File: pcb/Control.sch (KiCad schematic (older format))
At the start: 13 parts, among them U1 ATMEGA328, U2 FT231X, Y1 Cristal

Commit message: carga de hojas jerarquia
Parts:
- added C11: 4,7u, symbol CP1
- added C12, C15: 100n, symbol C
- added U?: PCA9685, symbol PCA9685
- D1, D2: value LED -> Rojo; Fabricante (none) -> KINGBRIGHT ELECTRONIC; Provedor (none) -> tme; Ref (none) -> KP-2012EC; Ref_Proveedor (none) -> KP-2012EC
- R4, R5: value R -> 270; Fabricante (none) -> vishay; Provedor (none) -> tme; Ref (none) -> CRCW0805270RFKTABC; Ref_Proveedor (none) -> CRCW0805270RFKTABC
- U1: symbol ATMEGA328 -> ATMEGA328-RESCUE-ATMEGA328_Motor_Board; Fabricante (none) -> atmel; Provedor (none) -> tme; Ref (none) -> ATMEGA328P-AU; Ref_Proveedor (none) -> ATMEGA328P-AU
- U2: Fabricante (none) -> ftdi; Provedor (none) -> tme; Ref (none) -> FT231XS-R; Ref_Proveedor (none) -> FT231XS-R
- Y1: value Cristal -> 16MHz; Proveedor (none) -> tme; Ref. Proveedor (none) -> EEVFK1J471M
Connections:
- wire segments 80 -> 91
- no-connect marks 10 -> 8
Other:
- note added: "Rx"
- note added: "Tx"
- moved on the sheet: C2, C3, D1, D2, R1, R2, R3, R4, R5, U2, Y1

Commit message: finalizada realizacion de esquema
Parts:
- removed C1: CP1, symbol CP1
- removed C11: 4,7u, symbol CP1
- added C1: 4,7u, symbol CP
- added C3, C6: CP, symbol CP
- added C4: 100n, symbol C
- added R2, R3: 1K, symbol R
- added R4: 10K, symbol R
- added SW1: Pulsador_4p, symbol Pulsador_4p
- gave numbers to parts that had none: 1
- renumbered C15 to C5, C12 to C7, C3 to C8, R2 to R5, R3 to R6, R4 to R7, R5 to R8, U2 to U3
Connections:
- net labels added: ENC1_A2, ENC1_B2, ENC2_A2, ENC2_B2, MOTOR1_CURRENT, MOTOR2_CURRENT, MOTOR3_CURRENT, MOTOR4_CURRENT, PWM_OE, SCL, SDA, SERVO1, SERVO2, SERVO3, SERVO4
- net labels removed: CONSIGNA3, CONSIGNA4, DIO_1, DIO_2, DIO_3, DIO_4, DIO_5, DIO_6, DIO_7, DIO_8, MOTOR1_SENSE, MOTOR2_SENSE, MOTOR3_SENSE, MOTOR4_SENSE
- wire segments 91 -> 122
- no-connect marks 8 -> 13
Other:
- moved on the sheet: C2, R1, R5, R6, U1, U2, Y1

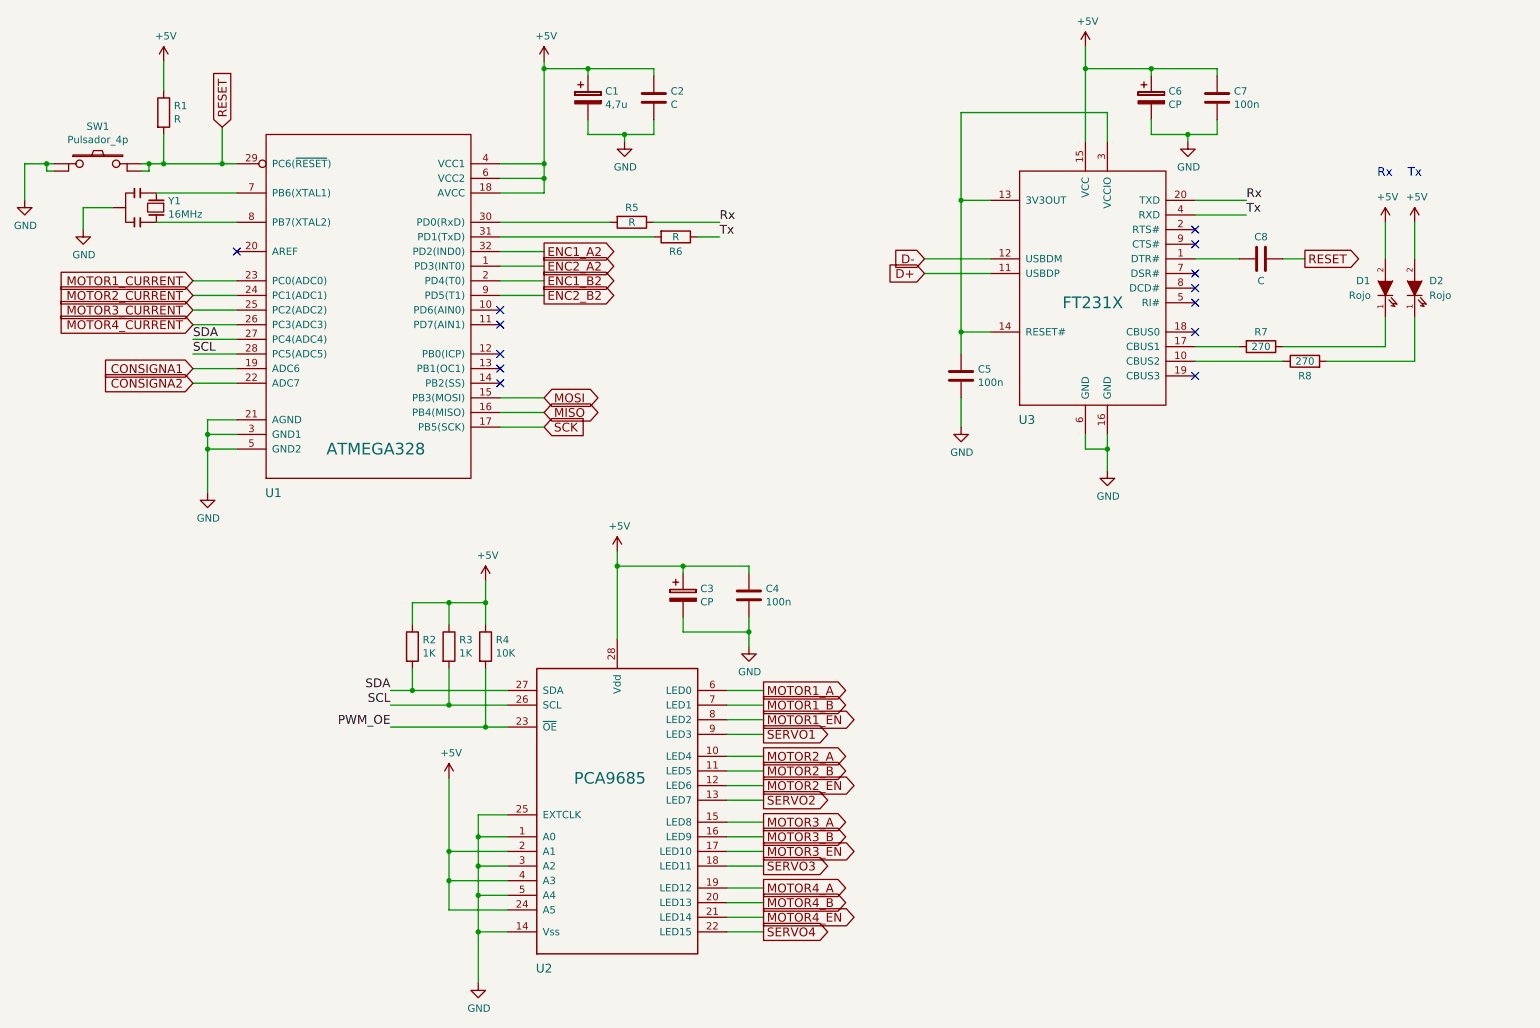
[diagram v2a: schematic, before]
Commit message: asociacion de huellas a resistencias y condensadores
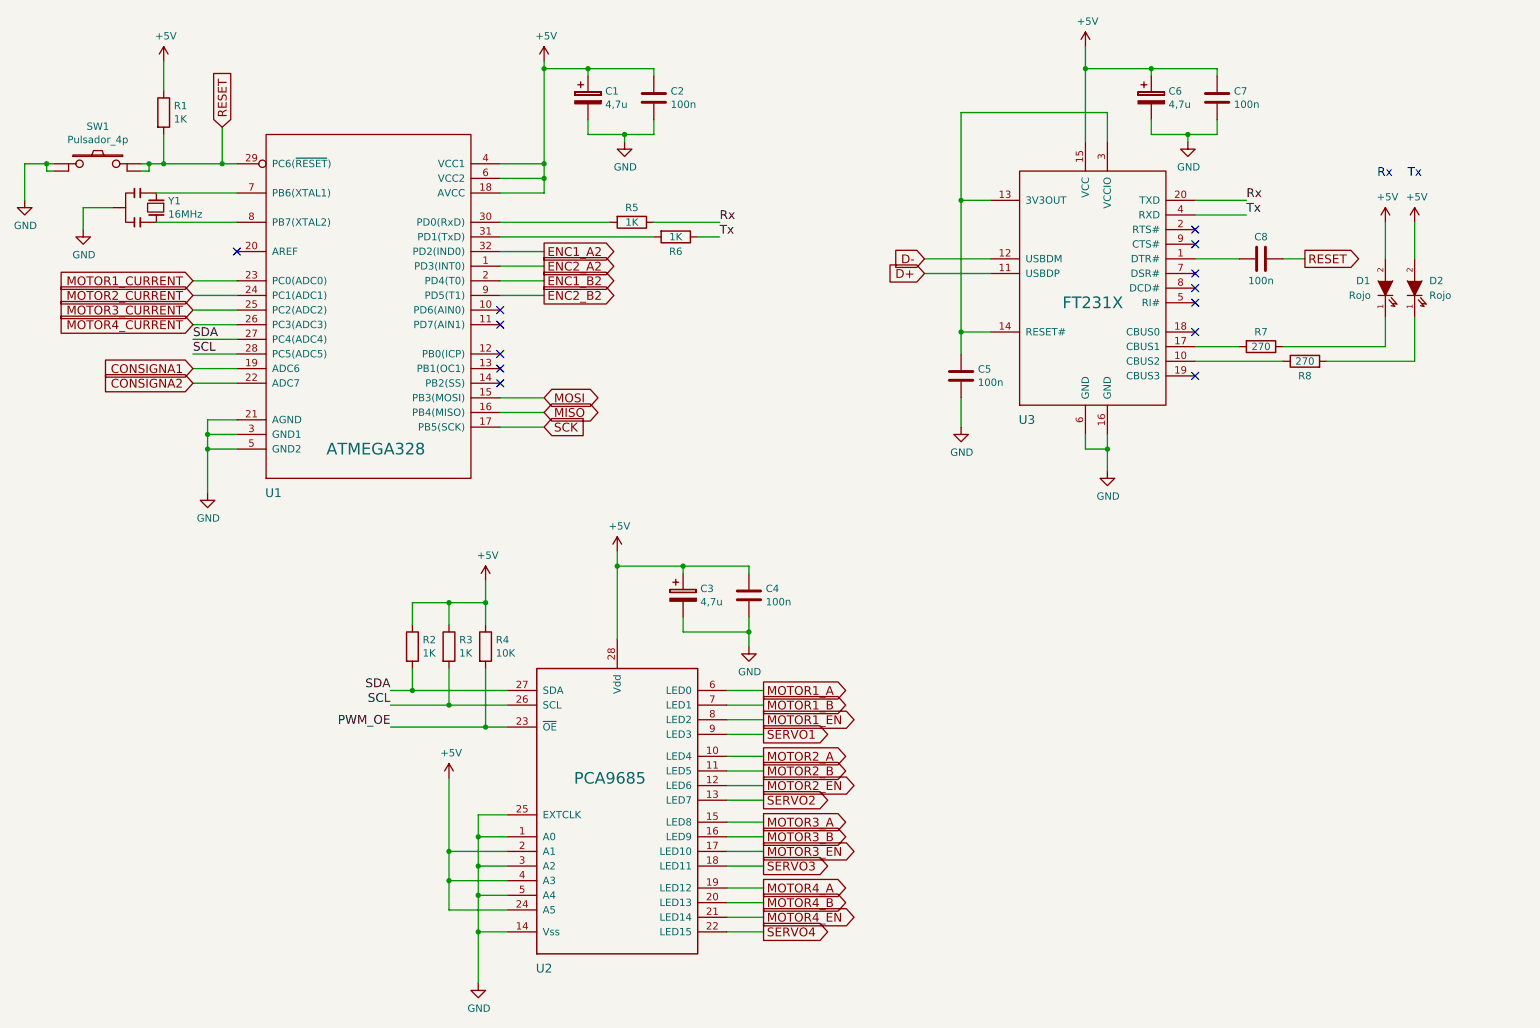
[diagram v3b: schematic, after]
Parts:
- C1: footprint (none) -> Capacitors_Tantalum_SMD:TantalC_SizeD_EIA-7343_Wave
- C2: value C -> 100n; footprint (none) -> Capacitors_SMD:C_0805; Fabricante (none) -> avx; Provedor (none) -> tme; Ref (none) -> 08055C104K4T2A; Ref_Proveedor (none) -> 08055C104K4T2A
- C3: value CP -> 4,7u; footprint (none) -> Capacitors_Tantalum_SMD:TantalC_SizeD_EIA-7343_Wave; Fabricante (none) -> avx; Provedor (none) -> tme; Ref (none) -> TAJD475K050RNJ; Ref_Proveedor (none) -> TAJD475K050R
- C4: footprint (none) -> Capacitors_SMD:C_0805; Fabricante (none) -> avx; Provedor (none) -> tme; Ref (none) -> 08055C104K4T2A; Ref_Proveedor (none) -> 08055C104K4T2A
- C5, C7: footprint (none) -> Capacitors_SMD:C_0805; Fabricante (none) -> VISHAY; Provedor (none) -> tme; Ref (none) -> CRCW08051K00FKEA; Ref_Proveedor (none) -> CRCW08051K00FKEA
- C6: value CP -> 4,7u; footprint (none) -> Capacitors_Tantalum_SMD:TantalC_SizeD_EIA-7343_Wave
- C8: value C -> 100n; footprint (none) -> Capacitors_SMD:C_0805; Fabricante (none) -> VISHAY; Provedor (none) -> tme; Ref (none) -> CRCW08051K00FKEA; Ref_Proveedor (none) -> CRCW08051K00FKEA
- R1, R5, R6: value R -> 1K; footprint (none) -> Resistors_SMD:R_0805; Fabricante (none) -> VISHAY; Provedor (none) -> tme; Ref (none) -> CRCW08051K00FKEA; Ref_Proveedor (none) -> CRCW08051K00FKEA
- R2, R3: footprint (none) -> Resistors_SMD:R_0805; Fabricante (none) -> VISHAY; Provedor (none) -> tme; Ref (none) -> CRCW08051K00FKEA; Ref_Proveedor (none) -> CRCW08051K00FKEA
- R4: footprint (none) -> Resistors_SMD:R_0805; Fabricante (none) -> vishay; Potencia (none) -> 0.125W; Provedor (none) -> tme; Ref (none) -> CRCW080510K0FKEA; Ref_Proveedor (none) -> CRCW080510K0FKEA; Tolerancia (none) -> 1%
- R7, R8: footprint (none) -> Resistors_SMD:R_0805
- SW1: footprint (none) -> Relays_and_Contacts:ALP_SKQGAKE010
- U1: footprint (none) -> Housings_QFP:TQFP-32_7x7mm_Pitch0.8mm
- U2: footprint (none) -> Housings_SSOP:TSSOP-28_4.4x9.7mm_Pitch0.65mm
- U3: footprint (none) -> Housings_SSOP:SSOP-20_4.4x6.5mm_Pitch0.65mm

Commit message: añadidas asociaciones de condensadores y led
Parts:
- C1, C3, C6: footprint Capacitors_Tantalum_SMD:TantalC_SizeD_EIA-7343_Wave -> Condensadores:TantalC_SizeD_EIA-7343_Wave
- D1, D2: footprint (none) -> Leds:LED_0805
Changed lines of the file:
@@
 F 0 "D1" V 10050 2900 50  0000 R CNN
 F 1 "Rojo" V 9950 2950 50  0000 R CNN
-F 2 "" H 10000 2700 50  0001 C CNN
+F 2 "Leds:LED_0805" H 10000 2700 50  0001 C CNN
 F 3 "" H 10000 2700 50  0000 C CNN
 F 4 "KINGBRIGHT ELECTRONIC" H 1700 1050 60  0001 C CNN "Fabricante"
@@
 F 0 "D2" V 10250 2600 50  0000 R CNN
 F 1 "Rojo" V 10150 2600 50  0000 R CNN
-F 2 "" H 10200 2700 50  0001 C CNN
+F 2 "Leds:LED_0805" H 10200 2700 50  0001 C CNN
 F 3 "" H 10200 2700 50  0000 C CNN
 F 4 "KINGBRIGHT ELECTRONIC" H 1700 1050 60  0001 C CNN "Fabricante"
@@
 F 0 "C1" H 4668 1446 50  0000 L CNN
 F 1 "4,7u" H 4668 1355 50  0000 L CNN
-F 2 "Capacitors_Tantalum_SMD:TantalC_SizeD_EIA-7343_Wave" H 4588 1250 50  0001 C CNN
+F 2 "Condensadores:TantalC_SizeD_EIA-7343_Wave" H 4588 1250 50  0001 C CNN
 F 3 "" H 4550 1400 50  0000 C CNN
 F 4 "avx" H 4550 1400 60  0001 C CNN "Fabricante"
@@
 F 0 "C6" H 8518 1446 50  0000 L CNN
 F 1 "4,7u" H 8518 1355 50  0000 L CNN
-F 2 "Capacitors_Tantalum_SMD:TantalC_SizeD_EIA-7343_Wave" H 8438 1250 50  0001 C CNN
+F 2 "Condensadores:TantalC_SizeD_EIA-7343_Wave" H 8438 1250 50  0001 C CNN
 F 3 "" H 8400 1400 50  0000 C CNN
 F 4 "~" H 8400 1400 60  0001 C CNN "Fabricante"
@@
 F 0 "C3" H 5318 4846 50  0000 L CNN
 F 1 "4,7u" H 5318 4755 50  0000 L CNN
-F 2 "Capacitors_Tantalum_SMD:TantalC_SizeD_EIA-7343_Wave" H 5238 4650 50  0001 C CNN
+F 2 "Condensadores:TantalC_SizeD_EIA-7343_Wave" H 5238 4650 50  0001 C CNN
 F 3 "" H 5200 4800 50  0000 C CNN
 F 4 "avx" H 4550 1400 60  0001 C CNN "Fabricante"

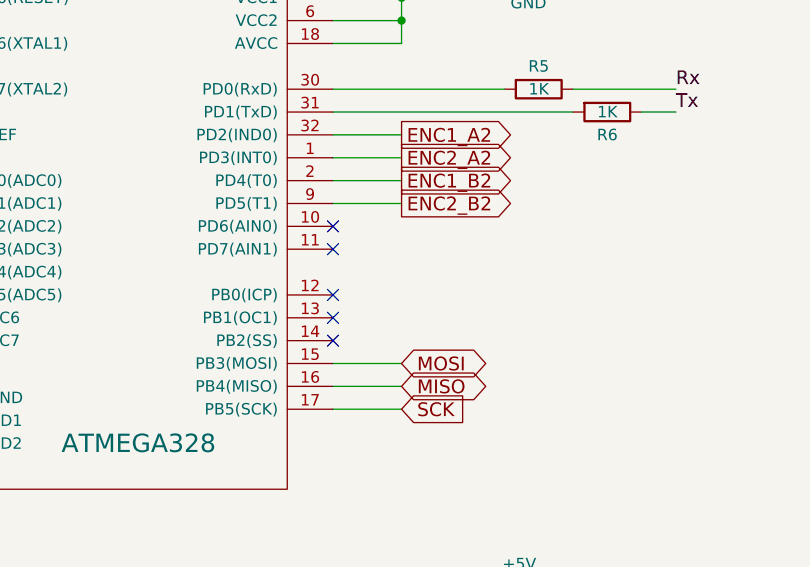
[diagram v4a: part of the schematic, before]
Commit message: Colocados todos los componenetes en el area. A revisar
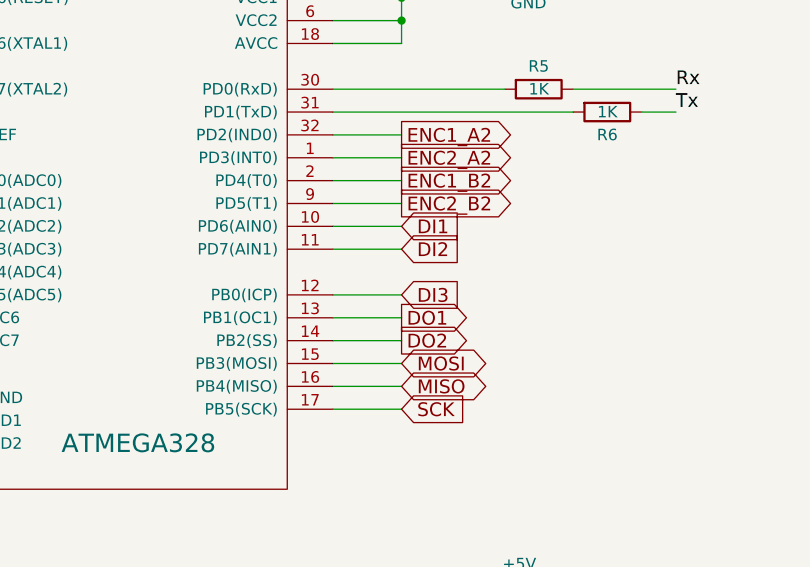
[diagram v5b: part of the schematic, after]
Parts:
- Y1: Fabricante (none) -> IQD FREQUENCY PRODUCTS; Ref (none) -> LF SPXO018034; Ref. Proveedor EEVFK1J471M -> CFPS-72-16M
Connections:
- net DI1: now reaches U1.10 (PD6(AIN0))
- net DI2: now reaches U1.11 (PD7(AIN1))
- net DI3: now reaches U1.12 (PB0(ICP))
- net DO1: now reaches U1.13 (PB1(OC1))
- net DO2: now reaches U1.14 (PB2(SS))
- no-connect marks 13 -> 8
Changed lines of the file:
@@
 F 2 "" H 2030 2260 50  0001 C CNN
 F 3 "" H 2030 2260 50  0000 C CNN
-F 4 "~" V 1600 2150 60  0001 C CNN "Fabricante"
-F 5 "~" V 1600 2150 60  0001 C CNN "Ref"
-F 6 "tme" V 1600 2150 60  0001 C CNN "Proveedor"
-F 7 "EEVFK1J471M" V 1600 2150 60  0001 C CNN "Ref. Proveedor"
+F 4 "IQD FREQUENCY PRODUCTS" V 1600 2150 60  0001 C CNN "Fabricante"
+F 5 "LF SPXO018034" V 1600 2150 60  0001 C CNN "Ref"
+F 6 "~" H 1600 2150 60  0001 C CNN "Potencia"
+F 7 "~" H 1600 2150 60  0001 C CNN "Tolerancia"
+F 8 "~" H 1600 2150 60  0001 C CNN "Provedor"
+F 9 "~" H 1600 2150 60  0001 C CNN "Ref_Proveedor"
+F 10 "tme" V 1600 2150 60  0001 C CNN "Proveedor"
+F 11 "CFPS-72-16M" V 1600 2150 60  0001 C CNN "Ref. Proveedor"
 	1    1600 2150
 	0    1    1    0
@@
 Text GLabel 4250 2750 2    60   Output ~ 0
 ENC2_B2
-NoConn ~ 3950 2850
-NoConn ~ 3950 2950
-NoConn ~ 3950 3150
-NoConn ~ 3950 3250
-NoConn ~ 3950 3350
 $Comp
 L Pulsador_4p SW1
@@
 	1    0    0    -1
 $EndComp
+Text GLabel 4250 2850 2    60   Input ~ 0
+DI1
+Text GLabel 4250 2950 2    60   Input ~ 0
+DI2
+Text GLabel 4250 3150 2    60   Input ~ 0
+DI3
+Text GLabel 4250 3250 2    60   Output ~ 0
+DO1
+Text GLabel 4250 3350 2    60   Output ~ 0
+DO2
+Wire Wire Line
+	3950 2850 4250 2850
+Wire Wire Line
+	4250 2950 3950 2950
+Wire Wire Line
+	3950 3150 4250 3150
+Wire Wire Line
+	4250 3250 3950 3250
+Wire Wire Line
+	3950 3350 4250 3350
 $EndSCHEMATC

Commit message: añadida huella para choke alimentacion
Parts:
- C1, C3: footprint Condensadores:TantalC_SizeD_EIA-7343_Wave -> Condensadores:TantalC_SizeC_EIA-6032_Wave; Ref TAJD475K050RNJ -> TAJC475K050RNJ; Ref_Proveedor TAJD475K050R -> TAJC475K050R
- C6: footprint Condensadores:TantalC_SizeD_EIA-7343_Wave -> Condensadores:TantalC_SizeC_EIA-6032_Wave; Fabricante (none) -> avx; Provedor (none) -> tme; Ref (none) -> TAJC475K050R; Ref_Proveedor (none) -> TAJC475K050RNJ
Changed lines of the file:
@@
 F 0 "C1" H 4668 1446 50  0000 L CNN
 F 1 "4,7u" H 4668 1355 50  0000 L CNN
-F 2 "Condensadores:TantalC_SizeD_EIA-7343_Wave" H 4588 1250 50  0001 C CNN
+F 2 "Condensadores:TantalC_SizeC_EIA-6032_Wave" H 4588 1250 50  0001 C CNN
 F 3 "" H 4550 1400 50  0000 C CNN
 F 4 "avx" H 4550 1400 60  0001 C CNN "Fabricante"
-F 5 "TAJD475K050RNJ" H 4550 1400 60  0001 C CNN "Ref"
+F 5 "TAJC475K050RNJ" H 4550 1400 60  0001 C CNN "Ref"
 F 6 "~" H 4550 1400 60  0001 C CNN "Potencia"
 F 7 "~" H 4550 1400 60  0001 C CNN "Tolerancia"
 F 8 "tme" H 4550 1400 60  0001 C CNN "Provedor"
-F 9 "TAJD475K050R" H 4550 1400 60  0001 C CNN "Ref_Proveedor"
+F 9 "TAJC475K050R" H 4550 1400 60  0001 C CNN "Ref_Proveedor"
 	1    4550 1400
 	1    0    0    -1
@@
 F 0 "C6" H 8518 1446 50  0000 L CNN
 F 1 "4,7u" H 8518 1355 50  0000 L CNN
-F 2 "Condensadores:TantalC_SizeD_EIA-7343_Wave" H 8438 1250 50  0001 C CNN
+F 2 "Condensadores:TantalC_SizeC_EIA-6032_Wave" H 8438 1250 50  0001 C CNN
 F 3 "" H 8400 1400 50  0000 C CNN
-F 4 "~" H 8400 1400 60  0001 C CNN "Fabricante"
-F 5 "~" H 8400 1400 60  0001 C CNN "Ref"
+F 4 "avx" H 8400 1400 60  0001 C CNN "Fabricante"
+F 5 "TAJC475K050R" H 8400 1400 60  0001 C CNN "Ref"
 F 6 "~" H 8400 1400 60  0001 C CNN "Potencia"
 F 7 "~" H 8400 1400 60  0001 C CNN "Tolerancia"
-F 8 "~" H 8400 1400 60  0001 C CNN "Provedor"
-F 9 "~" H 8400 1400 60  0001 C CNN "Ref_Proveedor"
+F 8 "tme" H 8400 1400 60  0001 C CNN "Provedor"
+F 9 "TAJC475K050RNJ" H 8400 1400 60  0001 C CNN "Ref_Proveedor"
 	1    8400 1400
 	1    0    0    -1
@@
 F 0 "C3" H 5318 4846 50  0000 L CNN
 F 1 "4,7u" H 5318 4755 50  0000 L CNN
-F 2 "Condensadores:TantalC_SizeD_EIA-7343_Wave" H 5238 4650 50  0001 C CNN
+F 2 "Condensadores:TantalC_SizeC_EIA-6032_Wave" H 5238 4650 50  0001 C CNN
 F 3 "" H 5200 4800 50  0000 C CNN
 F 4 "avx" H 4550 1400 60  0001 C CNN "Fabricante"
-F 5 "TAJD475K050RNJ" H 4550 1400 60  0001 C CNN "Ref"
+F 5 "TAJC475K050RNJ" H 4550 1400 60  0001 C CNN "Ref"
 F 6 "~" H 4550 1400 60  0001 C CNN "Potencia"
 F 7 "~" H 4550 1400 60  0001 C CNN "Tolerancia"
 F 8 "tme" H 4550 1400 60  0001 C CNN "Provedor"
-F 9 "TAJD475K050R" H 4550 1400 60  0001 C CNN "Ref_Proveedor"
+F 9 "TAJC475K050R" H 4550 1400 60  0001 C CNN "Ref_Proveedor"
 	1    5200 4800
 	1    0    0    -1
